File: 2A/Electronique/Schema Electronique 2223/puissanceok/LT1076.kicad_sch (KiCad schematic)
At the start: 10 parts

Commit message: update schematic
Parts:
- renumbered C601 to C?, C704 to C?, C602 to C?, C603 to C?, CR601 to CR?, L601 to L?, R603 to R?, R602 to R?, R601 to R?, U601 to U?

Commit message: debut assignation empreintes
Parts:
- C?: footprint (none) -> Capacitor_SMD:C_0603_1608Metric_Pad1.08x0.95mm_HandSolder
- C?: footprint Capacitor_SMD:CP_Elec_10x10.5 -> Capacitor_SMD:C_0603_1608Metric_Pad1.08x0.95mm_HandSolder
- L?: footprint Inductor_SMD:L_Wuerth_WE-PD-Typ-LS_Handsoldering -> Inductor_SMD:L_0805_2012Metric_Pad1.05x1.20mm_HandSolder
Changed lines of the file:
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@@
       (effects (font (size 1.27 1.27)) (justify left))
     )
-    (property "Footprint" "" (at 183.896 105.156 0)
+    (property "Footprint" "Capacitor_SMD:C_0603_1608Metric_Pad1.08x0.95mm_HandSolder" (at 183.896 105.156 0)
       (effects (font (size 1.27 1.27)) hide)
     )
@@
       (effects (font (size 1.27 1.27)) (justify left))
     )
-    (property "Footprint" "Capacitor_SMD:CP_Elec_10x10.5" (at 161.036 74.676 0)
+    (property "Footprint" "Capacitor_SMD:C_0603_1608Metric_Pad1.08x0.95mm_HandSolder" (at 161.036 74.676 0)
       (effects (font (size 1.27 1.27)) hide)
     )
@@
       (effects (font (size 1.27 1.27)))
     )
-    (property "Footprint" "Inductor_SMD:L_Wuerth_WE-PD-Typ-LS_Handsoldering" (at 149.606 68.326 0)
-      (effects (font (size 1.27 1.27)) hide)
-    )
+    (property "Footprint" "Inductor_SMD:L_0805_2012Metric_Pad1.05x1.20mm_HandSolder" (at 149.606 68.326 0)
+      (effects (font (size 1.27 1.27)) hide)
+    )

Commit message: update pcd
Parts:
- C? (x2): footprint Capacitor_SMD:C_0603_1608Metric_Pad1.08x0.95mm_HandSolder -> (none)
- C? (x2): footprint Capacitor_SMD:C_0603_1608Metric_Pad1.08x0.95mm_HandSolder -> Capacitor_SMD:C_0402_1005Metric
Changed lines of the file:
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@@
       (effects (font (size 1.27 1.27)) (justify left))
     )
-    (property "Footprint" "Capacitor_SMD:C_0603_1608Metric_Pad1.08x0.95mm_HandSolder" (at 106.1212 78.486 0)
+    (property "Footprint" "" (at 106.1212 78.486 0)
       (effects (font (size 1.27 1.27)) hide)
     )
@@
       (effects (font (size 1.27 1.27)) (justify left))
     )
-    (property "Footprint" "Capacitor_SMD:C_0603_1608Metric_Pad1.08x0.95mm_HandSolder" (at 183.896 105.156 0)
+    (property "Footprint" "Capacitor_SMD:C_0402_1005Metric" (at 183.896 105.156 0)
       (effects (font (size 1.27 1.27)) hide)
     )
@@
       (project "puissanceok"
         (path "/50648b18-b1a7-4d76-a5dd-1fad5f3e825e/d0016765-fb7e-4c4e-9d8c-f91c29732bdf"
-          (reference "#PWR035") (unit 1)
-        )
-        (path "/50648b18-b1a7-4d76-a5dd-1fad5f3e825e/7ec9b85e-02d5-4657-bc47-51feb658e8df"
-          (reference "#PWR042") (unit 1)
+          (reference "#PWR037") (unit 1)
+        )
+        (path "/50648b18-b1a7-4d76-a5dd-1fad5f3e825e/7ec9b85e-02d5-4657-bc47-51feb658e8df"
+          (reference "#PWR044") (unit 1)
         )
       )
@@
       (effects (font (size 1.27 1.27)) (justify left))
     )
-    (property "Footprint" "Capacitor_SMD:C_0603_1608Metric_Pad1.08x0.95mm_HandSolder" (at 110.236 93.726 0)
+    (property "Footprint" "Capacitor_SMD:C_0402_1005Metric" (at 110.236 93.726 0)
       (effects (font (size 1.27 1.27)) hide)
     )
@@
       (project "puissanceok"
         (path "/50648b18-b1a7-4d76-a5dd-1fad5f3e825e/d0016765-fb7e-4c4e-9d8c-f91c29732bdf"
-          (reference "C4") (unit 1)
-        )
-        (path "/50648b18-b1a7-4d76-a5dd-1fad5f3e825e/7ec9b85e-02d5-4657-bc47-51feb658e8df"
-          (reference "C10") (unit 1)
+          (reference "C5") (unit 1)
+        )
+        (path "/50648b18-b1a7-4d76-a5dd-1fad5f3e825e/7ec9b85e-02d5-4657-bc47-51feb658e8df"
+          (reference "C11") (unit 1)
         )
       )
@@
       (project "puissanceok"
         (path "/50648b18-b1a7-4d76-a5dd-1fad5f3e825e/d0016765-fb7e-4c4e-9d8c-f91c29732bdf"
-          (reference "#PWR033") (unit 1)
-        )
-        (path "/50648b18-b1a7-4d76-a5dd-1fad5f3e825e/7ec9b85e-02d5-4657-bc47-51feb658e8df"
-          (reference "#PWR040") (unit 1)
+          (reference "#PWR036") (unit 1)
+        )
+        (path "/50648b18-b1a7-4d76-a5dd-1fad5f3e825e/7ec9b85e-02d5-4657-bc47-51feb658e8df"
+          (reference "#PWR043") (unit 1)
         )
       )
@@
       (project "puissanceok"
         (path "/50648b18-b1a7-4d76-a5dd-1fad5f3e825e/d0016765-fb7e-4c4e-9d8c-f91c29732bdf"
-          (reference "#PWR032") (unit 1)
-        )
-        (path "/50648b18-b1a7-4d76-a5dd-1fad5f3e825e/7ec9b85e-02d5-4657-bc47-51feb658e8df"
-          (reference "#PWR039") (unit 1)
+          (reference "#PWR035") (unit 1)
+        )
+        (path "/50648b18-b1a7-4d76-a5dd-1fad5f3e825e/7ec9b85e-02d5-4657-bc47-51feb658e8df"
+          (reference "#PWR042") (unit 1)
         )
       )
@@
       (project "puissanceok"
         (path "/50648b18-b1a7-4d76-a5dd-1fad5f3e825e/d0016765-fb7e-4c4e-9d8c-f91c29732bdf"
-          (reference "R8") (unit 1)
-        )
-        (path "/50648b18-b1a7-4d76-a5dd-1fad5f3e825e/7ec9b85e-02d5-4657-bc47-51feb658e8df"
-          (reference "R15") (unit 1)
+          (reference "R7") (unit 1)
+        )
+        (path "/50648b18-b1a7-4d76-a5dd-1fad5f3e825e/7ec9b85e-02d5-4657-bc47-51feb658e8df"
+          (reference "R14") (unit 1)
         )
       )
@@
       (project "puissanceok"
         (path "/50648b18-b1a7-4d76-a5dd-1fad5f3e825e/d0016765-fb7e-4c4e-9d8c-f91c29732bdf"
-          (reference "#FLG02") (unit 1)
-        )
-        (path "/50648b18-b1a7-4d76-a5dd-1fad5f3e825e/7ec9b85e-02d5-4657-bc47-51feb658e8df"
           (reference "#FLG03") (unit 1)
+        )
+        (path "/50648b18-b1a7-4d76-a5dd-1fad5f3e825e/7ec9b85e-02d5-4657-bc47-51feb658e8df"
+          (reference "#FLG04") (unit 1)
         )
       )
@@
       (project "puissanceok"
         (path "/50648b18-b1a7-4d76-a5dd-1fad5f3e825e/d0016765-fb7e-4c4e-9d8c-f91c29732bdf"
-          (reference "R7") (unit 1)
-        )
-        (path "/50648b18-b1a7-4d76-a5dd-1fad5f3e825e/7ec9b85e-02d5-4657-bc47-51feb658e8df"
-          (reference "R14") (unit 1)
+          (reference "R8") (unit 1)
+        )
+        (path "/50648b18-b1a7-4d76-a5dd-1fad5f3e825e/7ec9b85e-02d5-4657-bc47-51feb658e8df"
+          (reference "R15") (unit 1)
         )
       )
@@
       (project "puissanceok"
         (path "/50648b18-b1a7-4d76-a5dd-1fad5f3e825e/d0016765-fb7e-4c4e-9d8c-f91c29732bdf"
-          (reference "#PWR031") (unit 1)
-        )
-        (path "/50648b18-b1a7-4d76-a5dd-1fad5f3e825e/7ec9b85e-02d5-4657-bc47-51feb658e8df"
-          (reference "#PWR038") (unit 1)
+          (reference "#PWR033") (unit 1)
+        )
+        (path "/50648b18-b1a7-4d76-a5dd-1fad5f3e825e/7ec9b85e-02d5-4657-bc47-51feb658e8df"
+          (reference "#PWR040") (unit 1)
         )
       )
@@
       (effects (font (size 1.27 1.27)) (justify left))
     )
-    (property "Footprint" "Capacitor_SMD:C_0603_1608Metric_Pad1.08x0.95mm_HandSolder" (at 161.036 74.676 0)
+    (property "Footprint" "" (at 161.036 74.676 0)
       (effects (font (size 1.27 1.27)) hide)
     )
@@
       (project "puissanceok"
         (path "/50648b18-b1a7-4d76-a5dd-1fad5f3e825e/d0016765-fb7e-4c4e-9d8c-f91c29732bdf"
-          (reference "C5") (unit 1)
-        )
-        (path "/50648b18-b1a7-4d76-a5dd-1fad5f3e825e/7ec9b85e-02d5-4657-bc47-51feb658e8df"
-          (reference "C11") (unit 1)
-        )
-      )
+          (reference "C4") (unit 1)
+        )
+        (path "/50648b18-b1a7-4d76-a5dd-1fad5f3e825e/7ec9b85e-02d5-4657-bc47-51feb658e8df"
+          (reference "C10") (unit 1)
+        )
+      )

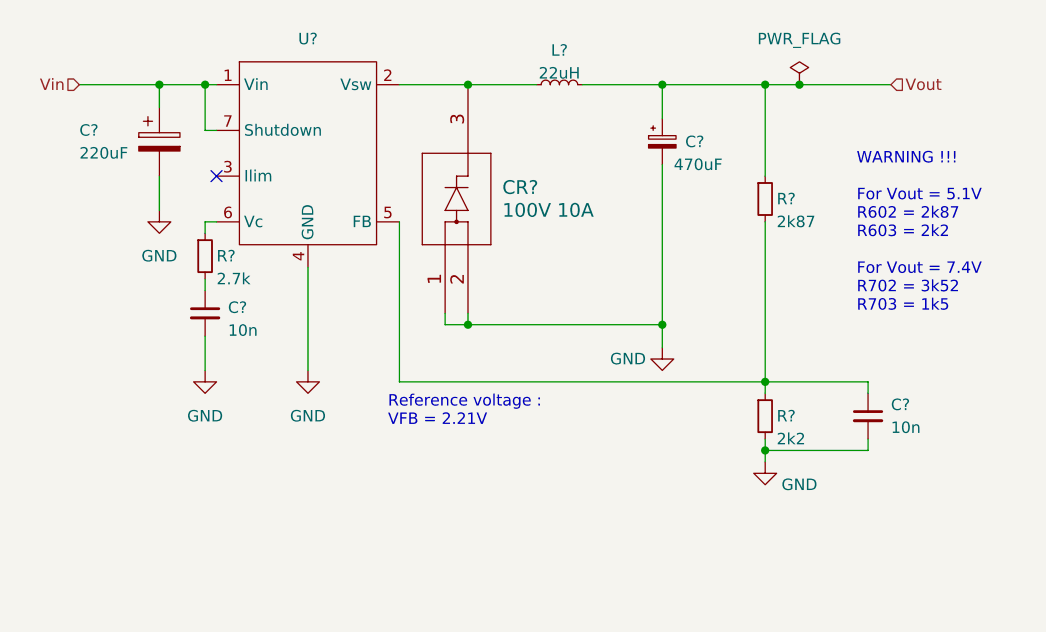
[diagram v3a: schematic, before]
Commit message: add schematic update and footprint
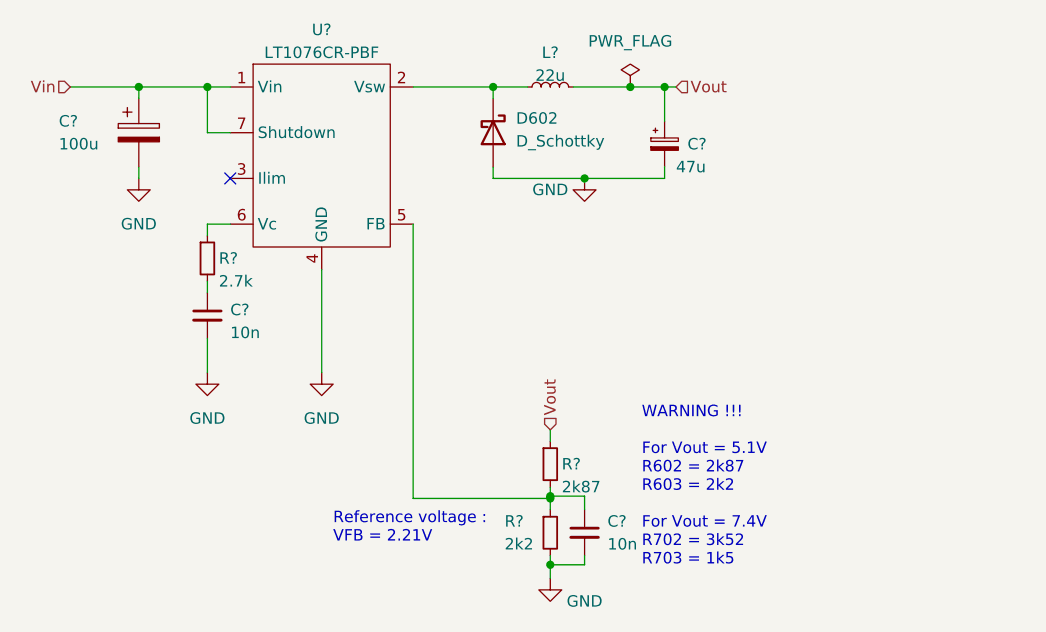
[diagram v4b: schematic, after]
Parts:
- removed CR?: 100V 10A, symbol custom:DST10100S
- added D602: D_Schottky, custom:DST10100S, symbol Device:D_Schottky
- C?: value 220uF -> 100u; footprint (none) -> Capacitor_SMD:CP_Elec_6.3x7.7; MPN (none) -> 865060445005; Vmax (none) -> 25V
- C?: value 470uF -> 47u; footprint (none) -> Capacitor_SMD:CP_Elec_6.3x5.4; MFR 865060457009 -> 865060543005
- L?: value 22uH -> 22u; footprint Inductor_SMD:L_0805_2012Metric_Pad1.05x1.20mm_HandSolder -> Inductor_SMD:L_Changjiang_FNR8065S
- U?: value ~ -> LT1076CR-PBF; footprint (none) -> Package_TO_SOT_SMD:TO-263-7_TabPin4
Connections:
- net GND: now also D602.2 (A)
- net at L?.1, U?.2 (Vsw): now also D602.1 (K)
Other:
- moved on the sheet: C?, L?, R?, U?

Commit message: finalize schematic + footprints
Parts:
- L?: value 22u -> 22m
- R? (x3): footprint Resistor_SMD:R_0603_1608Metric_Pad0.98x0.95mm_HandSolder -> Resistor_SMD:R_0402_1005Metric
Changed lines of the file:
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@@
       (effects (font (size 1.27 1.27)) (justify left))
     )
-    (property "Footprint" "Resistor_SMD:R_0603_1608Metric_Pad0.98x0.95mm_HandSolder" (at 148.59 118.11 0)
+    (property "Footprint" "Resistor_SMD:R_0402_1005Metric" (at 148.59 118.11 0)
       (effects (font (size 1.27 1.27)) hide)
     )
@@
       (effects (font (size 1.27 1.27)) (justify left))
     )
-    (property "Footprint" "Resistor_SMD:R_0603_1608Metric_Pad0.98x0.95mm_HandSolder" (at 148.59 110.49 0)
+    (property "Footprint" "Resistor_SMD:R_0402_1005Metric" (at 148.59 110.49 0)
       (effects (font (size 1.27 1.27)) hide)
     )
@@
       (effects (font (size 1.27 1.27)) (justify left))
     )
-    (property "Footprint" "Resistor_SMD:R_0603_1608Metric_Pad0.98x0.95mm_HandSolder" (at 110.49 87.63 0)
+    (property "Footprint" "Resistor_SMD:R_0402_1005Metric" (at 110.49 87.63 0)
       (effects (font (size 1.27 1.27)) hide)
     )
@@
       (effects (font (size 1.27 1.27)))
     )
-    (property "Value" "22u" (at 148.59 67.31 90)
-      (effects (font (size 1.27 1.27)))
-    )
+    (property "Value" "22m" (at 148.59 67.31 90)
+      (effects (font (size 1.27 1.27)))
+    )
